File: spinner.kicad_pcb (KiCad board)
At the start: 2 copper layers, 190 x 190 mm, 87 parts, among them J1 Micro_SD_Card, SW1 SW_SPDT, U1 AP63205WU, U2 RS0102, U3 SFH617A-3X006, U4 SFH617A-3X006, U5 SFH617A-3X006

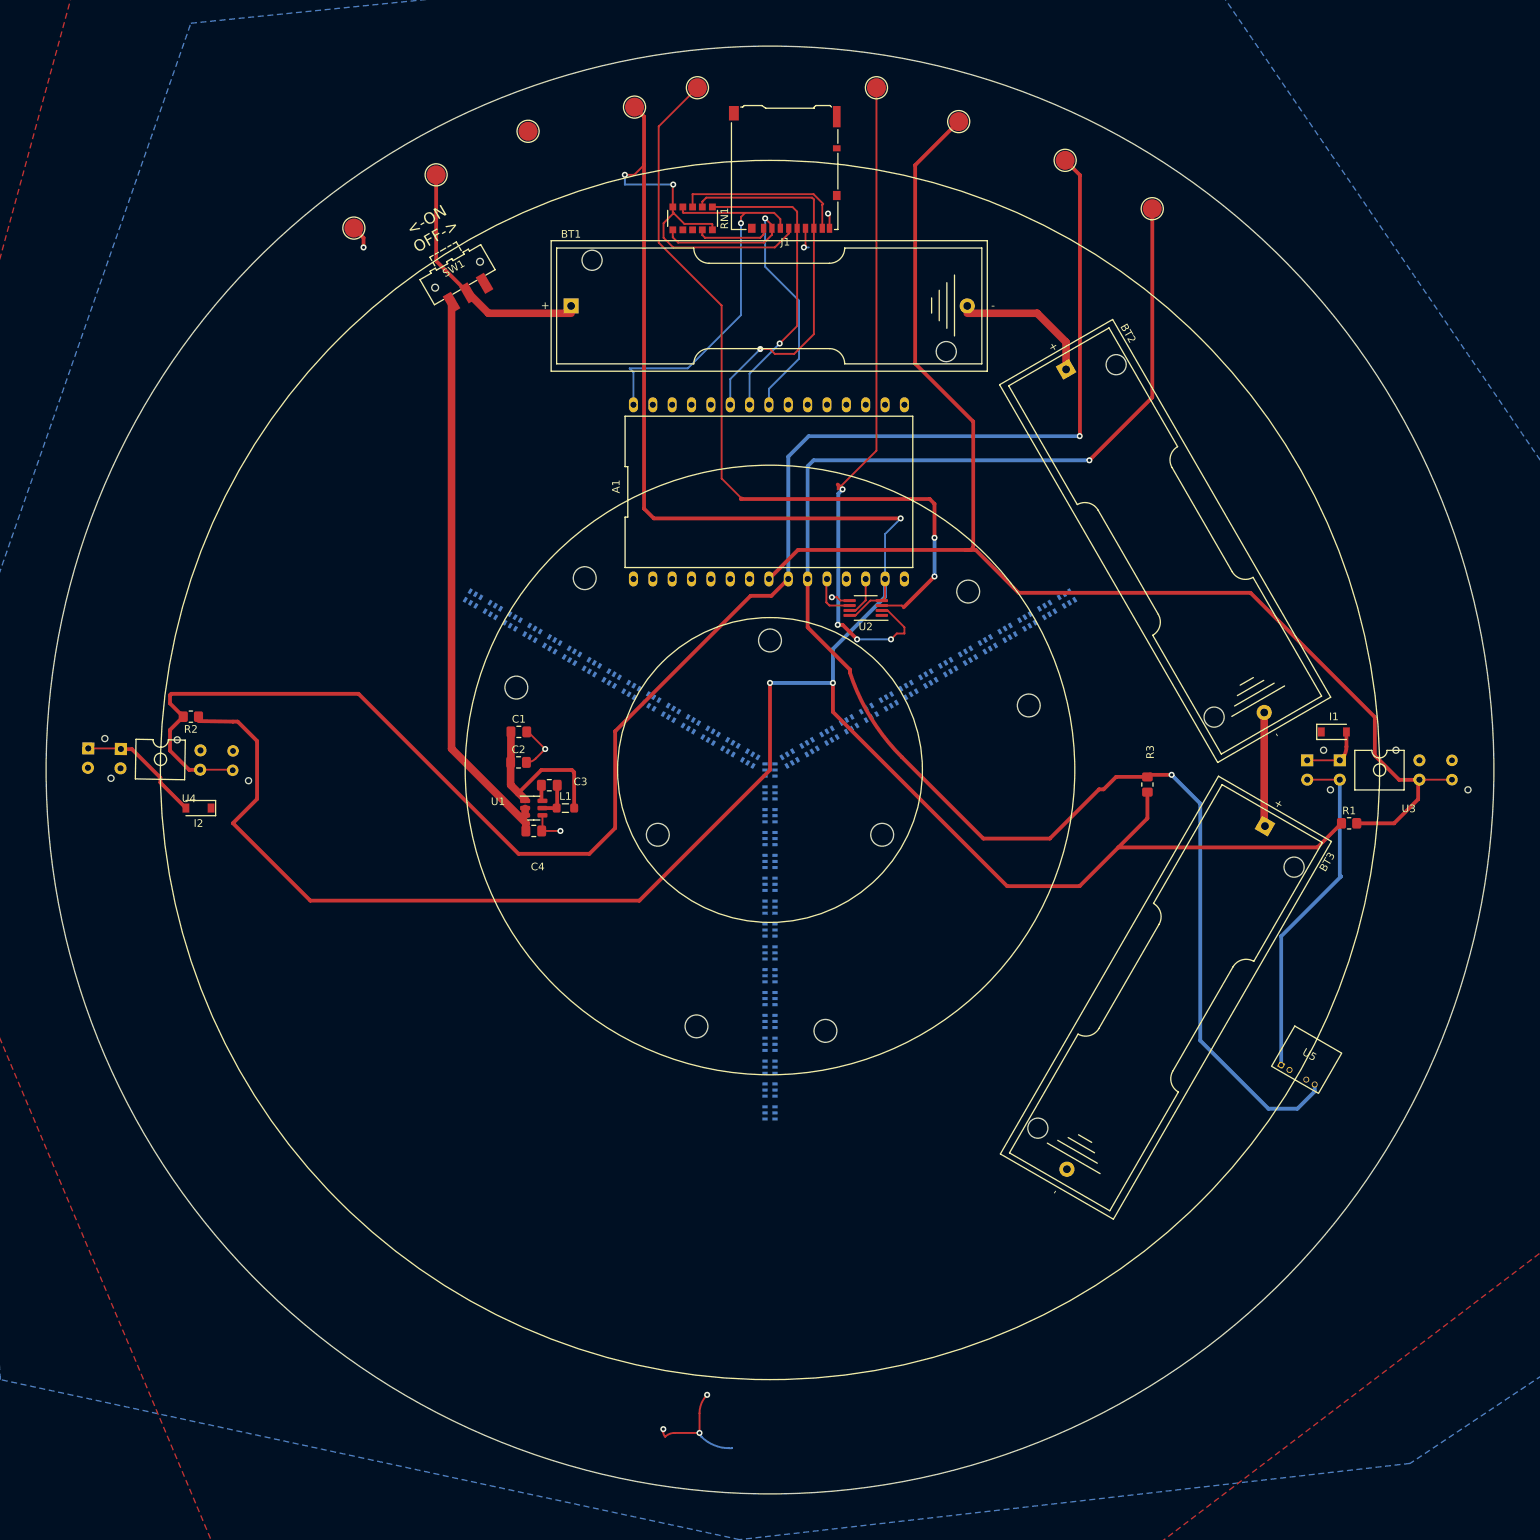
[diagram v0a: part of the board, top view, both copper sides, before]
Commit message: Place more LEDs.  Not quite done.
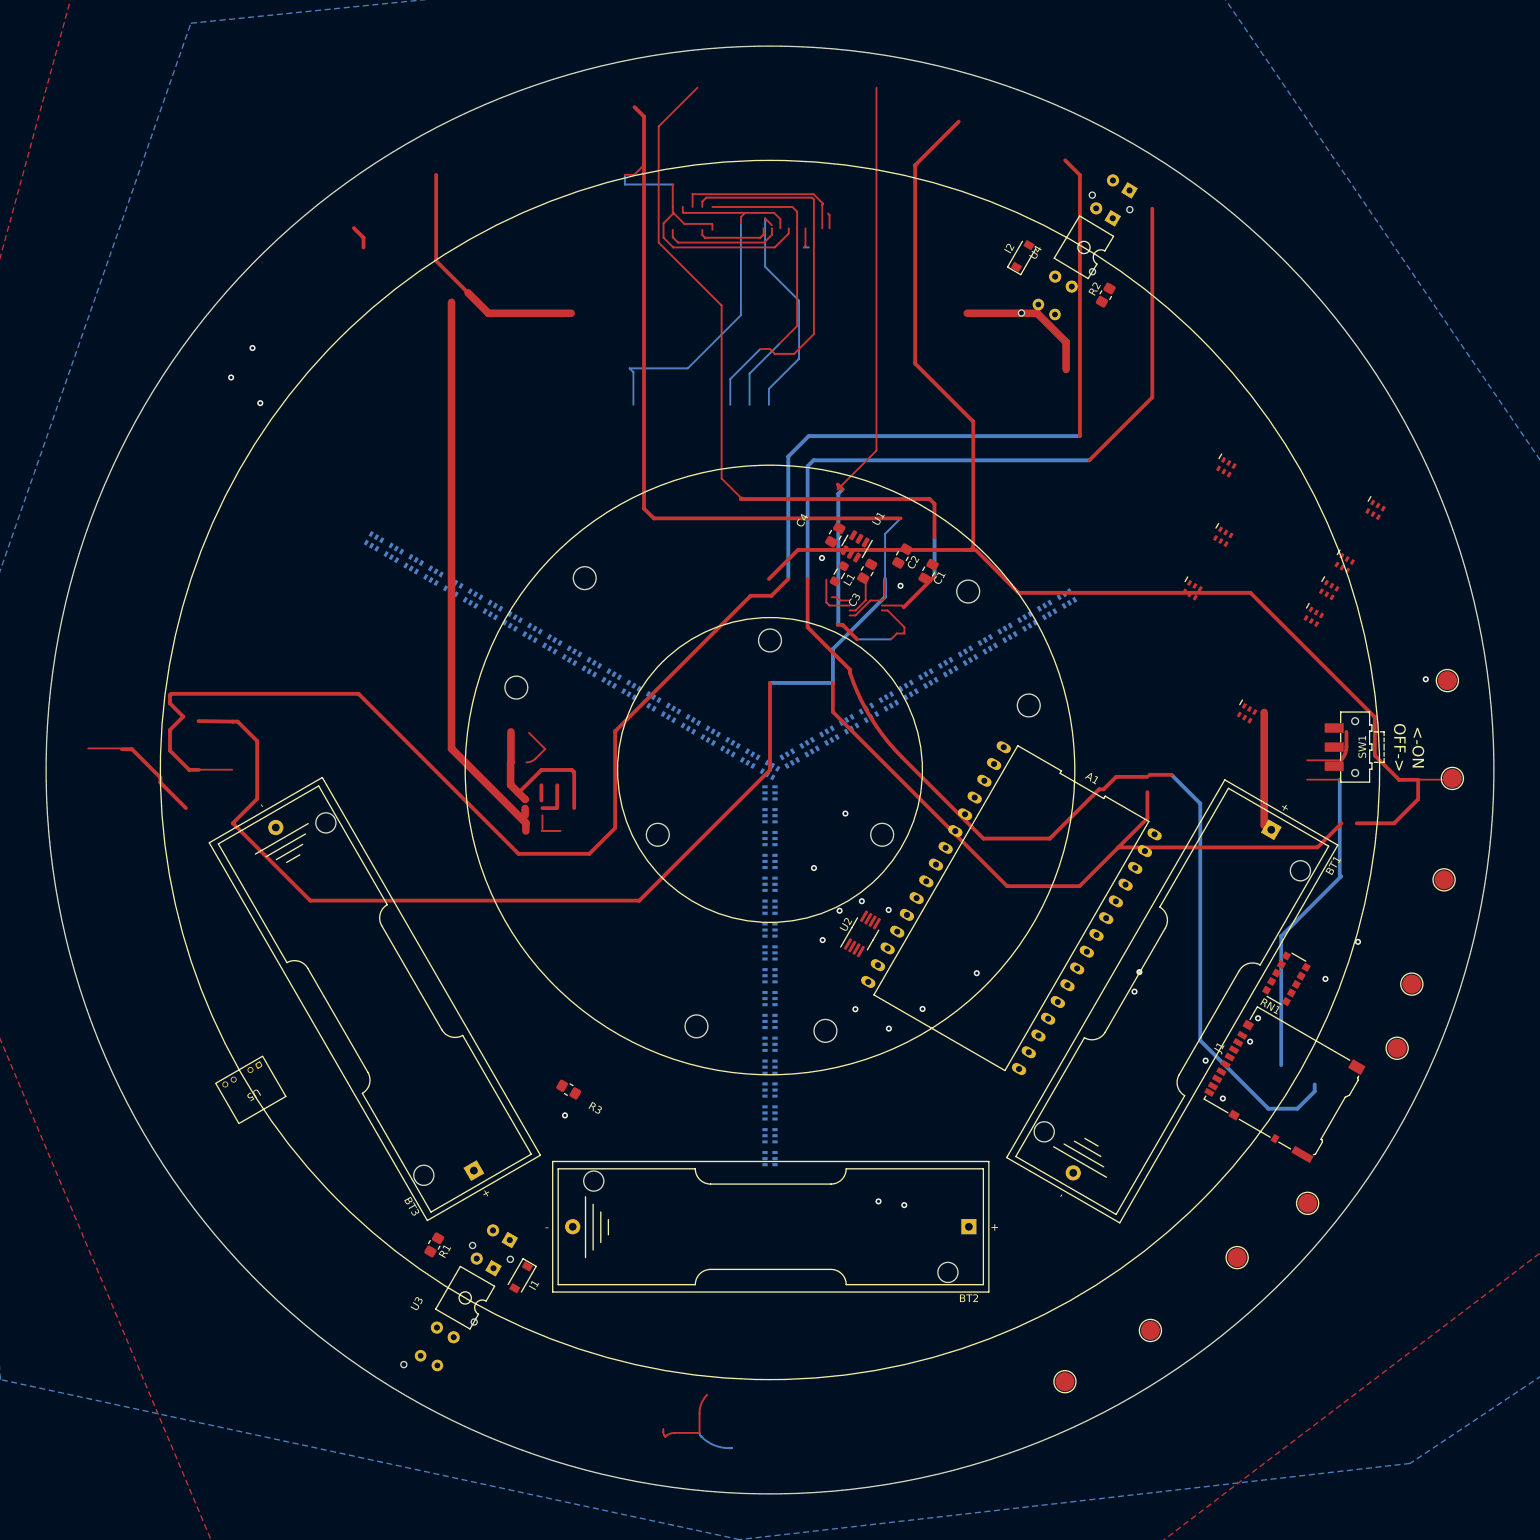
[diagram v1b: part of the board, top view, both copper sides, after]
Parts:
- added D116: APA102, Library:SK9822-hakz, B.Cu at (108.4, 76.0)
- added D117: APA102, Library:SK9822-hakz, B.Cu at (105.8, 74.5)
- added D118: APA102, Library:SK9822-hakz, B.Cu at (103.2, 73.0)
- added D119: APA102, Library:SK9822-hakz, B.Cu at (100.6, 71.5)
- added D120: APA102, Library:SK9822-hakz, B.Cu at (98.0, 70.0)
- added D216: APA102, Library:SK9822-hakz, F.Cu at (205.4, 76.4)
- added D217: APA102, Library:SK9822-hakz, F.Cu at (223.4, 76.4)
- added D218: APA102, Library:SK9822-hakz, F.Cu at (221.4, 79.9)
- added D219: APA102, Library:SK9822-hakz, F.Cu at (212.6, 92.6)
- added D220: APA102, Library:SK9822-hakz, F.Cu at (209.5, 69.4)
- added D316: APA102, Library:SK9822-hakz, B.Cu at (150.0, 148.0)
- added D317: APA102, Library:SK9822-hakz, B.Cu at (150.0, 151.0)
- added D318: APA102, Library:SK9822-hakz, F.Cu at (209.9, 60.3)
- added D319: APA102, Library:SK9822-hakz, F.Cu at (225.4, 72.9)
- added D320: APA102, Library:SK9822-hakz, F.Cu at (229.5, 65.9)
- moved TP5 157.0 mm to (220.6, 156.9), turned to -120 degrees
- moved TP1 156.0 mm to (232.3, 136.5), turned to -120 degrees
- moved TP2 155.3 mm to (238.9, 88.3), turned to -120 degrees
- moved TP4 155.2 mm to (238.5, 114.4), turned to -120 degrees
- moved TP9 155.1 mm to (239.5, 101.1), turned to -120 degrees
- moved TP6 154.4 mm to (188.7, 180.3), turned to -120 degrees
- moved TP7 154.0 mm to (199.9, 173.6), turned to -120 degrees
- moved TP3 153.8 mm to (234.2, 128.1), turned to -120 degrees
- moved TP8 153.5 mm to (211.3, 164.0), turned to -120 degrees
- moved U4 138.6 mm to (191.2, 31.4), turned to -121 degrees
- moved U3 138.6 mm to (110.0, 169.3), turned to -120 degrees
- moved U5 138.6 mm to (80.7, 140.0), turned to -150 degrees
- moved J1 136.6 mm to (217.3, 141.1), turned to 60 degrees
- moved SW1 133.1 mm to (226.8, 97.0), turned to 90 degrees
- moved R2 132.2 mm to (194.1, 37.7), turned to 60 degrees
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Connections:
- D115 pad 5: /CO_1 -> Net-(D115-Pad5)
- D115 pad 6: /DO_1 -> Net-(D115-Pad6)
- D215 pad 5: /CO_3 -> Net-(D215-Pad5)
- D215 pad 6: /DO_3 -> Net-(D215-Pad6)
- D315 pad 5: unconnected-(D315-Pad5) -> Net-(D315-Pad5)
- D315 pad 6: unconnected-(D315-Pad6) -> Net-(D315-Pad6)
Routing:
- net /OPTO_in_2: track 216.1 -> 179.7 mm
- net Net-(D315-Pad6): track 0.00 -> 36.4 mm
- net Net-(BT1-Pad2): track 18.1 -> 0.00 mm
- net /OPTO_in_1: track 222.5 -> 240.6 mm
- net +BATT: track 31.9 -> 46.7 mm
- net Net-(BT2-Pad2): track 14.8 -> 0.00 mm
- net /CI: track 104.5 -> 95.8 mm
- net GND: track 37.1 -> 45.8 mm
- net unconnected-(SW1-Pad1): track 0.00 -> 8.21 mm
- net Net-(I1-Pad2): track 8.21 -> 0.00 mm
- net Net-(C3-Pad1): track 4.79 -> 10.3 mm
- net /GPIO_13: track 5.47 -> 0.00 mm
